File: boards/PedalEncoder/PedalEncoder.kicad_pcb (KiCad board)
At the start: 2 copper layers, 125 x 38.5 mm, 35 parts, among them J1 Pwr, J2 Control, J3 Switch, J4 ISP, J5 Pedal, J6 MIDI Out, J7 I2C, Q1 BC547, Q2 BC547, U1 4069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

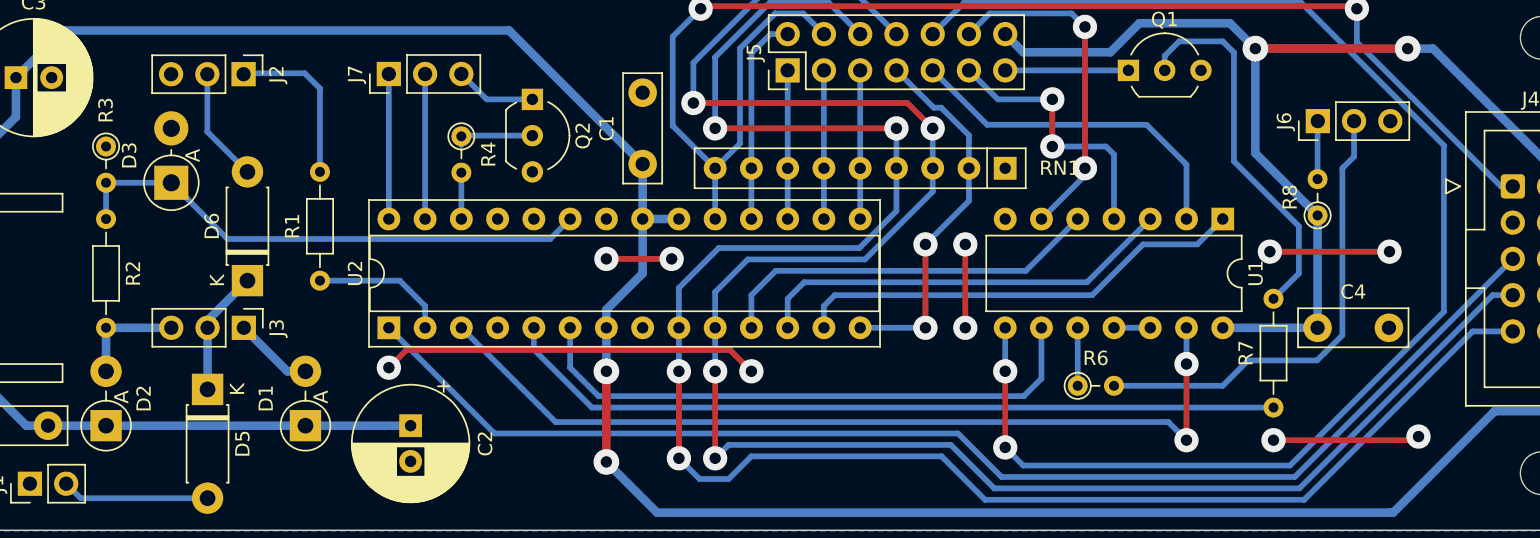
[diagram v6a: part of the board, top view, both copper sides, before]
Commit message: Updated design rules to 0.32mm template and exported Gerber files
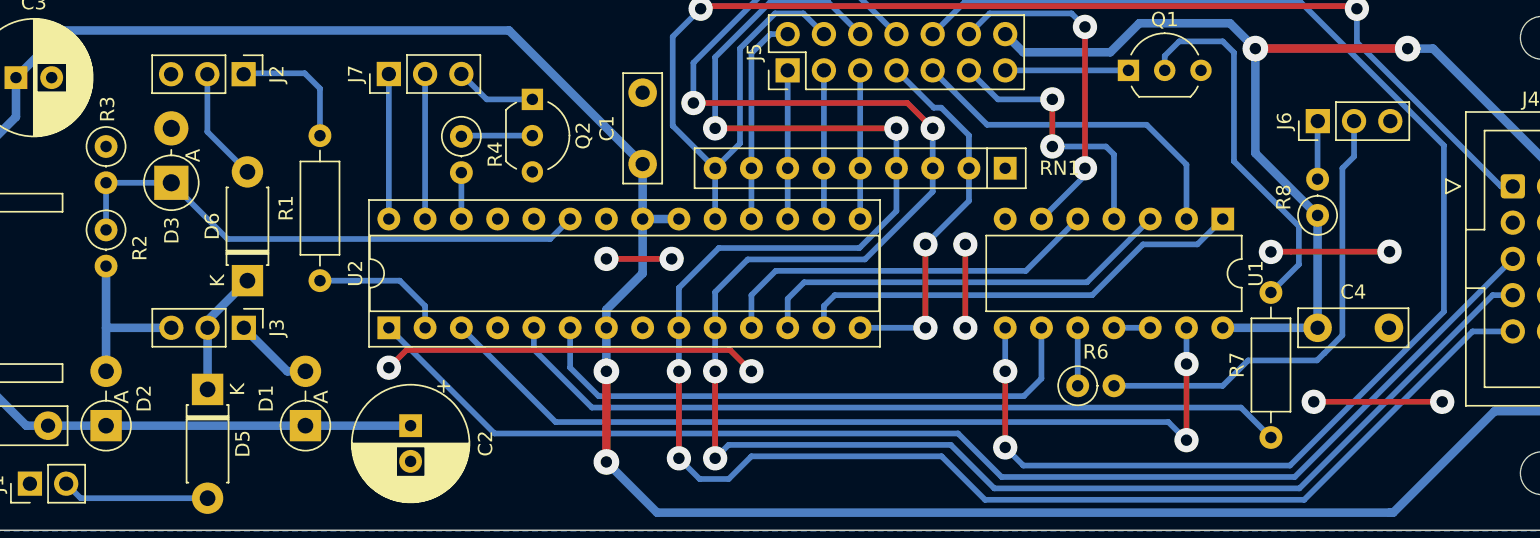
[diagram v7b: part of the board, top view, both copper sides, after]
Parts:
- R1, R7: footprint Resistor_THT:R_Axial_DIN0204_L3.6mm_D1.6mm_P7.62mm_Horizontal -> Resistor_THT:R_Axial_DIN0207_L6.3mm_D2.5mm_P10.16mm_Horizontal
- R2: footprint Resistor_THT:R_Axial_DIN0204_L3.6mm_D1.6mm_P7.62mm_Horizontal -> Resistor_THT:R_Axial_DIN0207_L6.3mm_D2.5mm_P2.54mm_Vertical
- R3, R4, R6, R8: footprint Resistor_THT:R_Axial_DIN0204_L3.6mm_D1.6mm_P2.54mm_Vertical -> Resistor_THT:R_Axial_DIN0207_L6.3mm_D2.5mm_P2.54mm_Vertical
- moved R7 2.11 mm to (170.0, 107.0)
- moved R2 0.76 mm to (88.4, 92.5)
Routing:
- net /PWR_CFG: track 7.11 -> 11.4 mm
- net Net-(J2-Pin_1): track 11.7 -> 9.12 mm
- net GND: track 55.6 -> 54.3 mm
- net PWM: track 55.0 -> 55.7 mm
- net Net-(Q2-B): track 5.61 -> 4.99 mm

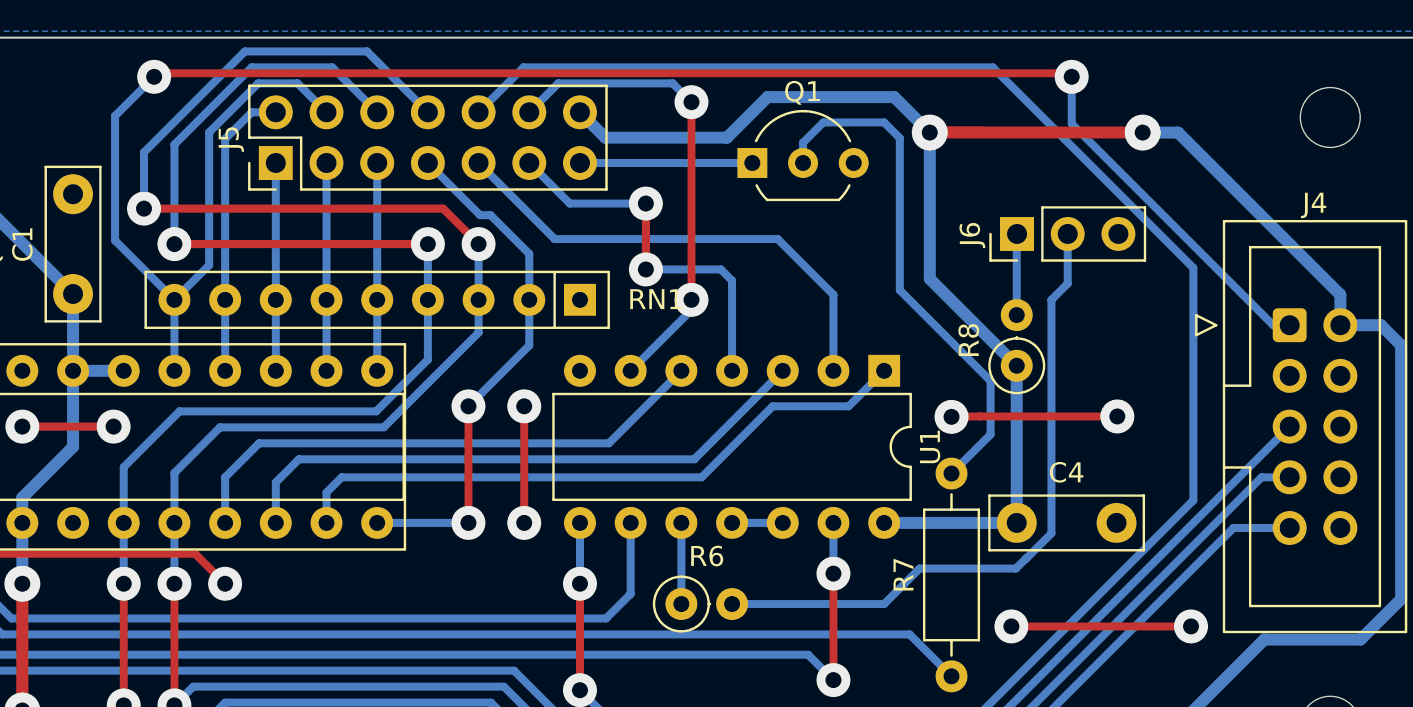
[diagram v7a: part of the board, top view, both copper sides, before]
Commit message: Fixed PedalEncoder ISP hedaer schematics, added Errata notes
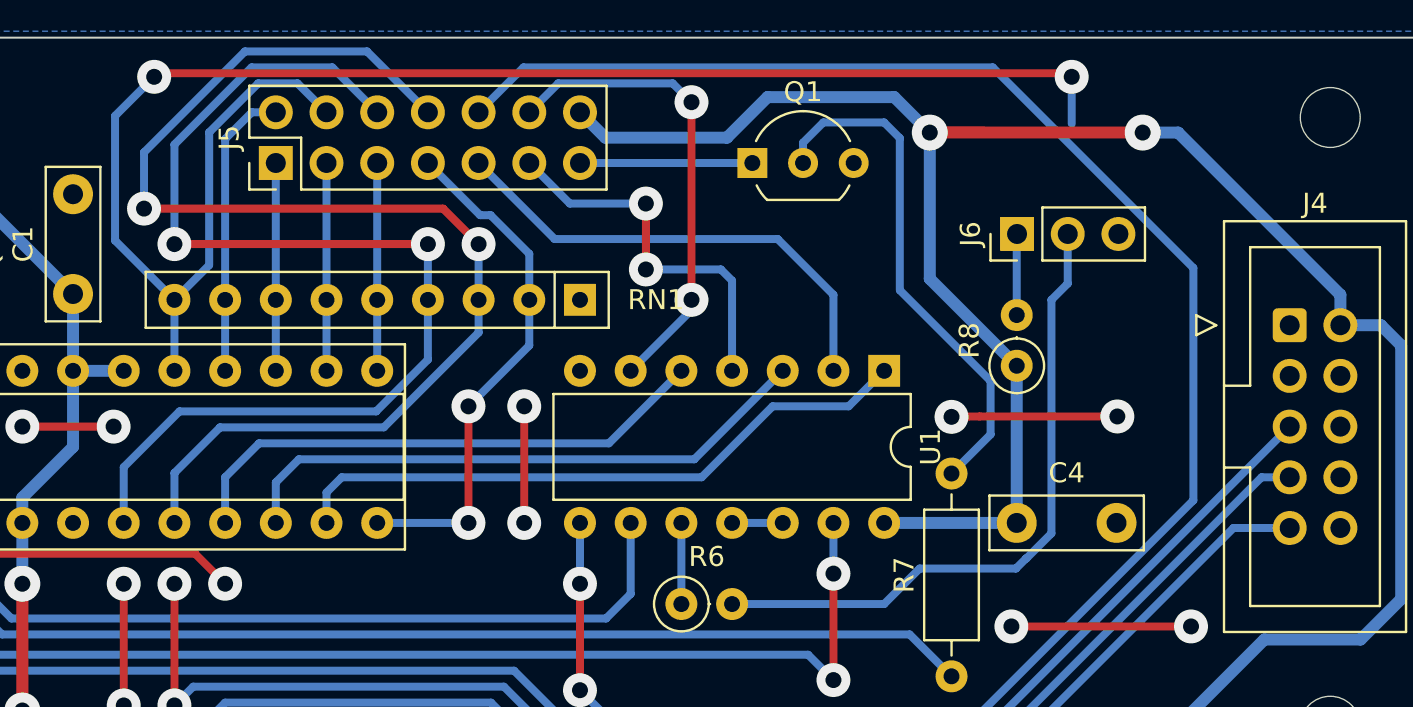
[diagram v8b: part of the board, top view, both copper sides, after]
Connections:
- J5 pad 1: Net-(J5-Pin_1) -> MOSI
- J5 pad 2: Net-(J5-Pin_2) -> MISO
- J5 pad 4: MOSI -> SCK
- J5 pad 6: MISO -> Net-(J5-Pin_6)
- J5 pad 8: SCK -> Net-(J5-Pin_8)
- RN1 pad 3: SCK -> Net-(J5-Pin_8)
- RN1 pad 4: MISO -> Net-(J5-Pin_6)
- RN1 pad 7: Net-(J5-Pin_1) -> MOSI
- RN1 pad 8: Net-(J5-Pin_2) -> MISO
- RN1 pad 9: MOSI -> SCK
- U2 pad 10: SCK -> Net-(J5-Pin_8)
- U2 pad 17: Net-(J5-Pin_1) -> MOSI
- U2 pad 18: Net-(J5-Pin_2) -> MISO
- U2 pad 19: MOSI -> SCK
- U2 pad 9: MISO -> Net-(J5-Pin_6)
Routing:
- net MOSI: track 97.0 -> 9.65 mm, vias 2 -> 0
- net Net-(J5-Pin_8): track 0.00 -> 62.5 mm, vias 0 -> 2
- net Net-(J5-Pin_6): track 0.00 -> 55.9 mm, vias 0 -> 2
- net MISO: track 130.9 -> 86.6 mm, vias 4 -> 2
- net SCK: track 134.8 -> 151.1 mm
- net Net-(J5-Pin_2): track 14.7 -> 0.00 mm
- net Net-(J5-Pin_1): track 9.65 -> 0.00 mm
